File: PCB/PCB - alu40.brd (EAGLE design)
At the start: 228 x 76 mm, 163 parts, among them IC1 XB3303ASOT23, IC2 TP4054-42-SOT25-R, J1 SK-3296S-01-L1, J2 USB4510-03-1-A, Q2 PMOSFET, Q3 PMOSFET, Q5 PMOSFET, Q6 NMOSFET, U1 ISP1807-LRISP1807-LR_ISP1807-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, X1 BM02B-SRSS-TB

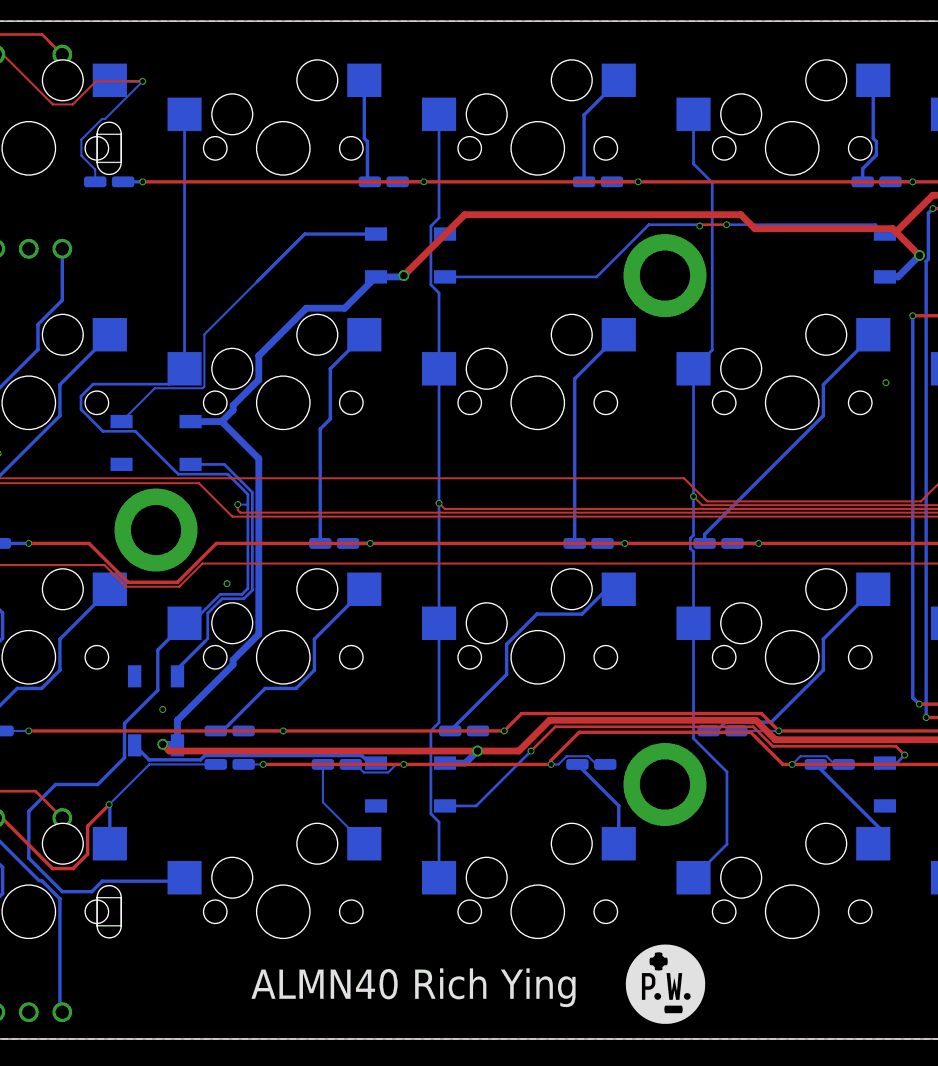
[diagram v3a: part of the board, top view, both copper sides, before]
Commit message: add silk, spare diodes, move D1
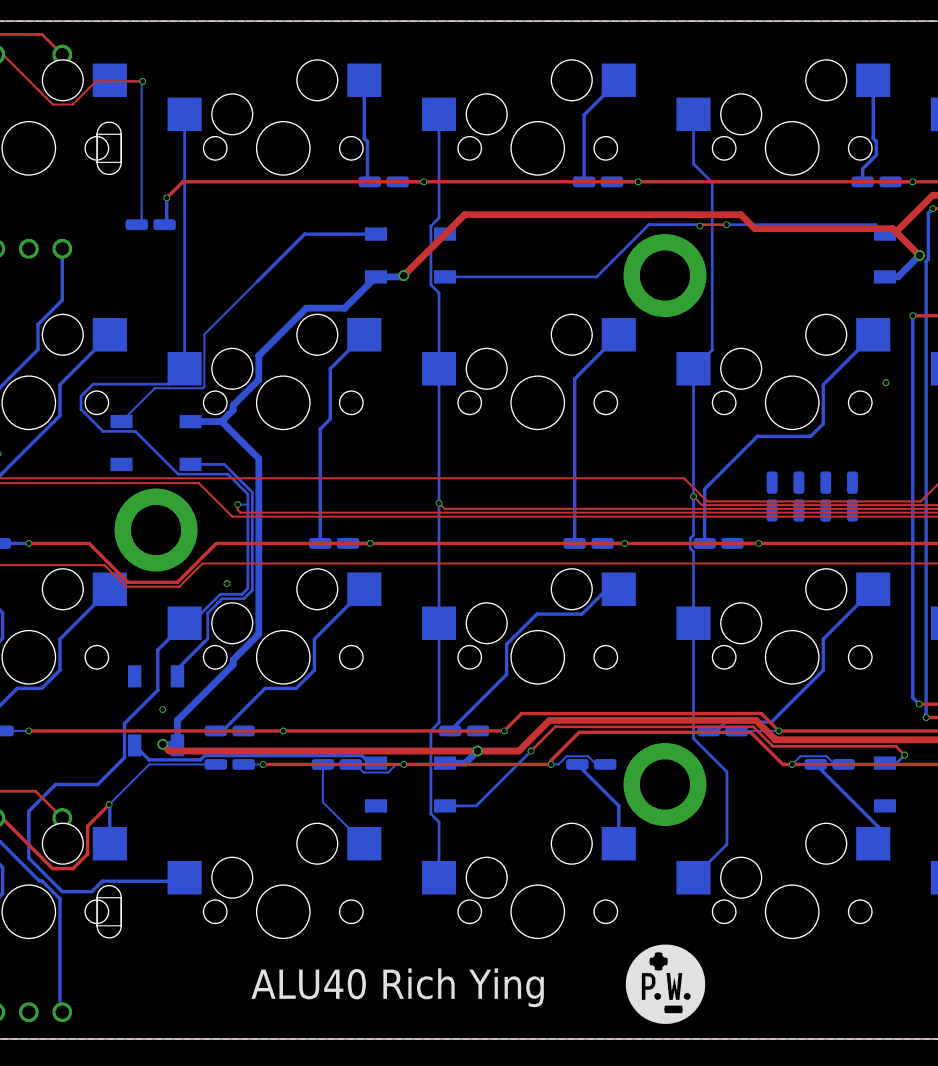
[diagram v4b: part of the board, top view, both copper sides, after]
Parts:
- added D49, D50, D51, D52: 1N4148WS, Volume_V1:SOD-323
- moved D1 4.46 mm to (18.6, 60.8)
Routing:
- net N$16: track 20.8 -> 23.1 mm
- net N$68: track 25.7 -> 26.6 mm
- net ROW0: track 240.4 -> 239.7 mm
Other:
- board text added: "+ -"
- board text added: "ALU40 Rich Ying"
- board text removed: "ALMN40 Rich Ying"
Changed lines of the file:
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@@
 <rectangle x1="83.7736" y1="36.781" x2="106.4812" y2="41.4546" layer="42"/>
 <wire x1="112" y1="22.5" x2="116" y2="22.5" width="2.54" layer="46"/>
-<text x="26.1" y="3" size="2.1844" layer="25">ALMN40 Rich Ying</text>
+<text x="26.1" y="3" size="2.1844" layer="25">ALU40 Rich Ying</text>
 <rectangle x1="56.8773" y1="1.127096875" x2="57.20241875" y2="1.132178125" layer="25"/>
 <rectangle x1="56.78078125" y1="1.132178125" x2="57.2989375" y2="1.137259375" layer="25"/>
@@
 <wire x1="112" y1="22.5" x2="116" y2="22.5" width="2.54" layer="41"/>
 <wire x1="112" y1="22.5" x2="116" y2="22.5" width="2.54" layer="42"/>
+<text x="138.7" y="55.9" size="2.54" layer="22" rot="MR90">+ -</text>
+<text x="160.4" y="57.6" size="2.54" layer="22" rot="MR90">+ -</text>
 </plain>
 <attributes>
@@
 </groups>
 <elements>
-<element name="D1" library="Volume_V1" library_urn="urn:adsk.eagle:library:32198814" package="SOD-323" package3d_urn="urn:adsk.eagle:package:32198954/3" value="1N4148WS" x="15.5" y="64" smashed="yes" rot="MR0" grouprefs="ALL">
-<attribute name="CREATED_BY" value="PCBLayout.com" x="15.5" y="64" size="1.778" layer="28" rot="MR0" display="off"/>
-<attribute name="DIGIKEY_PART_NUMBER" value="1N4148WSFSTR-ND" x="15.5" y="64" size="1.778" layer="28" rot="MR0" display="off"/>
-<attribute name="MANUFACTURER" value="Diodes Incorporated" x="15.5" y="64" size="1.778" layer="28" rot="MR0" display="off"/>
-<attribute name="MPN" value="1N4148WS" x="15.5" y="64" size="1.778" layer="28" rot="MR0" display="off"/>
-<attribute name="PACKAGE" value="SOD-323" x="15.5" y="64" size="1.778" layer="28" rot="MR0" display="off"/>
+<element name="D1" library="Volume_V1" library_urn="urn:adsk.eagle:library:32198814" package="SOD-323" package3d_urn="urn:adsk.eagle:package:32198954/3" value="1N4148WS" x="18.6" y="60.8" smashed="yes" rot="MR0" grouprefs="ALL">
+<attribute name="CREATED_BY" value="PCBLayout.com" x="18.6" y="60.8" size="1.778" layer="28" rot="MR0" display="off"/>
+<attribute name="DIGIKEY_PART_NUMBER" value="1N4148WSFSTR-ND" x="18.6" y="60.8" size="1.778" layer="28" rot="MR0" display="off"/>
+<attribute name="MANUFACTURER" value="Diodes Incorporated" x="18.6" y="60.8" size="1.778" layer="28" rot="MR0" display="off"/>
+<attribute name="MPN" value="1N4148WS" x="18.6" y="60.8" size="1.778" layer="28" rot="MR0" display="off"/>
+<attribute name="PACKAGE" value="SOD-323" x="18.6" y="60.8" size="1.778" layer="28" rot="MR0" display="off"/>
 </element>
 <element name="12" library="Volume_V1" library_urn="urn:adsk.eagle:library:32198814" package="CHERRY" package3d_urn="urn:adsk.eagle:package:32198958/1" value="" x="28.5" y="66.5" smashed="yes" rot="SR0" grouprefs="ALL"/>
@@
 <attribute name="VALUE" x="114" y="73.25" size="1.27" layer="28" rot="MR180" align="center"/>
 </element>
+<element name="D49" library="Volume_V1" library_urn="urn:adsk.eagle:library:32198814" package="SOD-323" package3d_urn="urn:adsk.eagle:package:32198954/3" value="1N4148WS" x="65" y="40.5" smashed="yes" rot="MR270">
+<attribute name="CREATED_BY" value="PCBLayout.com" x="65" y="40.5" size="2.54" layer="28" rot="MR270" display="off"/>
+<attribute name="DIGIKEY_PART_NUMBER" value="1N4148WSFSTR-ND" x="65" y="40.5" size="2.54" layer="28" rot="MR270" display="off"/>
+<attribute name="MANUFACTURER" value="Diodes Incorporated" x="65" y="40.5" size="2.54" layer="28" rot="MR270" display="off"/>
+<attribute name="MPN" value="1N4148WS" x="65" y="40.5" size="2.54" layer="28" rot="MR270" display="off"/>
+<attribute name="PACKAGE" value="SOD-323" x="65" y="40.5" size="2.54" layer="28" rot="MR270" display="off"/>
+</element>
+<element name="D50" library="Volume_V1" library_urn="urn:adsk.eagle:library:32198814" package="SOD-323" package3d_urn="urn:adsk.eagle:package:32198954/3" value="1N4148WS" x="67" y="40.5" smashed="yes" rot="MR270">
+<attribute name="CREATED_BY" value="PCBLayout.com" x="67" y="40.5" size="2.54" layer="28" rot="MR270" display="off"/>
+<attribute name="DIGIKEY_PART_NUMBER" value="1N4148WSFSTR-ND" x="67" y="40.5" size="2.54" layer="28" rot="MR270" display="off"/>
+<attribute name="MANUFACTURER" value="Diodes Incorporated" x="67" y="40.5" size="2.54" layer="28" rot="MR270" display="off"/>
+<attribute name="MPN" value="1N4148WS" x="67" y="40.5" size="2.54" layer="28" rot="MR270" display="off"/>
+<attribute name="PACKAGE" value="SOD-323" x="67" y="40.5" size="2.54" layer="28" rot="MR270" display="off"/>
+</element>
+<element name="D51" library="Volume_V1" library_urn="urn:adsk.eagle:library:32198814" package="SOD-323" package3d_urn="urn:adsk.eagle:package:32198954/3" value="1N4148WS" x="69" y="40.5" smashed="yes" rot="MR270">
+<attribute name="CREATED_BY" value="PCBLayout.com" x="69" y="40.5" size="2.54" layer="28" rot="MR270" display="off"/>
+<attribute name="DIGIKEY_PART_NUMBER" value="1N4148WSFSTR-ND" x="69" y="40.5" size="2.54" layer="28" rot="MR270" display="off"/>
+<attribute name="MANUFACTURER" value="Diodes Incorporated" x="69" y="40.5" size="2.54" layer="28" rot="MR270" display="off"/>
+<attribute name="MPN" value="1N4148WS" x="69" y="40.5" size="2.54" layer="28" rot="MR270" display="off"/>
+<attribute name="PACKAGE" value="SOD-323" x="69" y="40.5" size="2.54" layer="28" rot="MR270" display="off"/>
+</element>
+<element name="D52" library="Volume_V1" library_urn="urn:adsk.eagle:library:32198814" package="SOD-323" package3d_urn="urn:adsk.eagle:package:32198954/3" value="1N4148WS" x="71" y="40.5" smashed="yes" rot="MR270">
+<attribute name="CREATED_BY" value="PCBLayout.com" x="71" y="40.5" size="2.54" layer="28" rot="MR270" display="off"/>
+<attribute name="DIGIKEY_PART_NUMBER" value="1N4148WSFSTR-ND" x="71" y="40.5" size="2.54" layer="28" rot="MR270" display="off"/>
+<attribute name="MANUFACTURER" value="Diodes Incorporated" x="71" y="40.5" size="2.54" layer="28" rot="MR270" display="off"/>
+<attribute name="MPN" value="1N4148WS" x="71" y="40.5" size="2.54" layer="28" rot="MR270" display="off"/>
+<attribute name="PACKAGE" value="SOD-323" x="71" y="40.5" size="2.54" layer="28" rot="MR270" display="off"/>
+</element>
 </elements>
 <signals>
@@
 <contactref element="D16" pad="A"/>
 <wire x1="72.55" y1="52.58" x2="68.8241" y2="48.8541" width="0.254" layer="16"/>
-<wire x1="68.8241" y1="48.8541" x2="68.8241" y2="46.537325" width="0.254" layer="16"/>
-<wire x1="59.96" y1="37.673225" x2="59.96" y2="37" width="0.254" layer="16"/>
-<wire x1="68.8241" y1="46.537325" x2="59.96" y2="37.673225" width="0.254" layer="16"/>
+<wire x1="68.8241" y1="48.8541" x2="68.8241" y2="45.937325" width="0.254" layer="16"/>
+<wire x1="68.8241" y1="45.937325" x2="67.886775" y2="45" width="0.254" layer="16"/>
+<wire x1="67.886775" y1="45" x2="63.9" y2="45" width="0.254" layer="16"/>
+<wire x1="63.9" y1="45" x2="59.96" y2="41.06" width="0.254" layer="16"/>
+<wire x1="59.96" y1="41.06" x2="59.96" y2="37" width="0.254" layer="16"/>
 </signal>
 <signal name="N$17">
@@
 <wire x1="18" y1="71.5" x2="15.63" y2="71.5" width="0.1524" layer="16"/>
 <wire x1="15.63" y1="71.5" x2="15.55" y2="71.58" width="0.1524" layer="16"/>
-<wire x1="18" y1="71.5" x2="15.19355" y2="68.69355" width="0.1524" layer="16"/>
-<wire x1="14.42701875" y1="64.9496625" x2="14.46" y2="64.8925375" width="0.1524" layer="16"/>
-<wire x1="14.46" y1="64.8925375" x2="14.46" y2="64" width="0.1524" layer="16"/>
-<wire x1="15.19355" y1="68.69355" x2="14.96925625" y2="68.69355" width="0.1524" layer="16"/>
-<wire x1="13.4243" y1="65.95238125" x2="14.42701875" y2="64.9496625" width="0.1524" layer="16"/>
-<wire x1="14.96925625" y1="68.69355" x2="13.4243" y2="67.14859375" width="0.1524" layer="16"/>
-<wire x1="13.4243" y1="67.14859375" x2="13.4243" y2="65.95238125" width="0.1524" layer="16"/>
+<wire x1="18" y1="71.5" x2="17.9243" y2="71.4243" width="0.1524" layer="16"/>
+<wire x1="17.9243" y1="71.4243" x2="17.9243" y2="61.1643" width="0.1524" layer="16"/>
+<wire x1="17.56" y1="60.8" x2="17.9243" y2="61.1643" width="0.1524" layer="16"/>
 </signal>
 <signal name="N$49">
@@
 <contactref element="D3" pad="C"/>
 <contactref element="D2" pad="C"/>
-<wire x1="16.54" y1="64" x2="18" y2="64" width="0.254" layer="16"/>
-<via x="18" y="64" extent="1-16" drill="0.35"/>
-<wire x1="18" y1="64" x2="39" y2="64" width="0.254" layer="1"/>
+<wire x1="19.8" y1="62.8" x2="19.8" y2="60.96" width="0.254" layer="16"/>
+<wire x1="19.8" y1="60.96" x2="19.64" y2="60.8" width="0.254" layer="16"/>
+<via x="19.8" y="62.8" extent="1-16" drill="0.35"/>
+<wire x1="39" y1="64" x2="21" y2="64" width="0.254" layer="1"/>
+<wire x1="21" y1="64" x2="19.8" y2="62.8" width="0.254" layer="1"/>
 <via x="95" y="64" extent="1-16" drill="0.35"/>
 <wire x1="39" y1="64" x2="55" y2="64" width="0.254" layer="1"/>
